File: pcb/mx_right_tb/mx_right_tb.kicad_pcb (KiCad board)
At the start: 2 copper layers, 134.9 x 113.3 mm, 60 parts, among them SW1 SW_PUSH, SW10 SW_PUSH, SW11 SW_PUSH, SW12 SW_PUSH, SW13 SW_PUSH, SW14 SW_PUSH, SW15 SW_PUSH, SW16 SW_PUSH, SW17 SW_PUSH, SW18 SW_PUSH, SW19 SW_PUSH, SW2 SW_PUSH, SW20 SW_PUSH, SW21 SW_PUSH, SW22 SW_PUSH, SW23 SW_PUSH, SW24 SW_PUSH, SW27 SW_PUSH, SW28 SW_PUSH, SW29 SW_PUSH, SW3 SW_PUSH, SW30 SW_PUSH, SW32 SW_SPDT, SW4 SW_PUSH, SW5 SW_PUSH, SW6 SW_PUSH, SW7 SW_PUSH, SW8 SW_PUSH, SW9 SW_PUSH

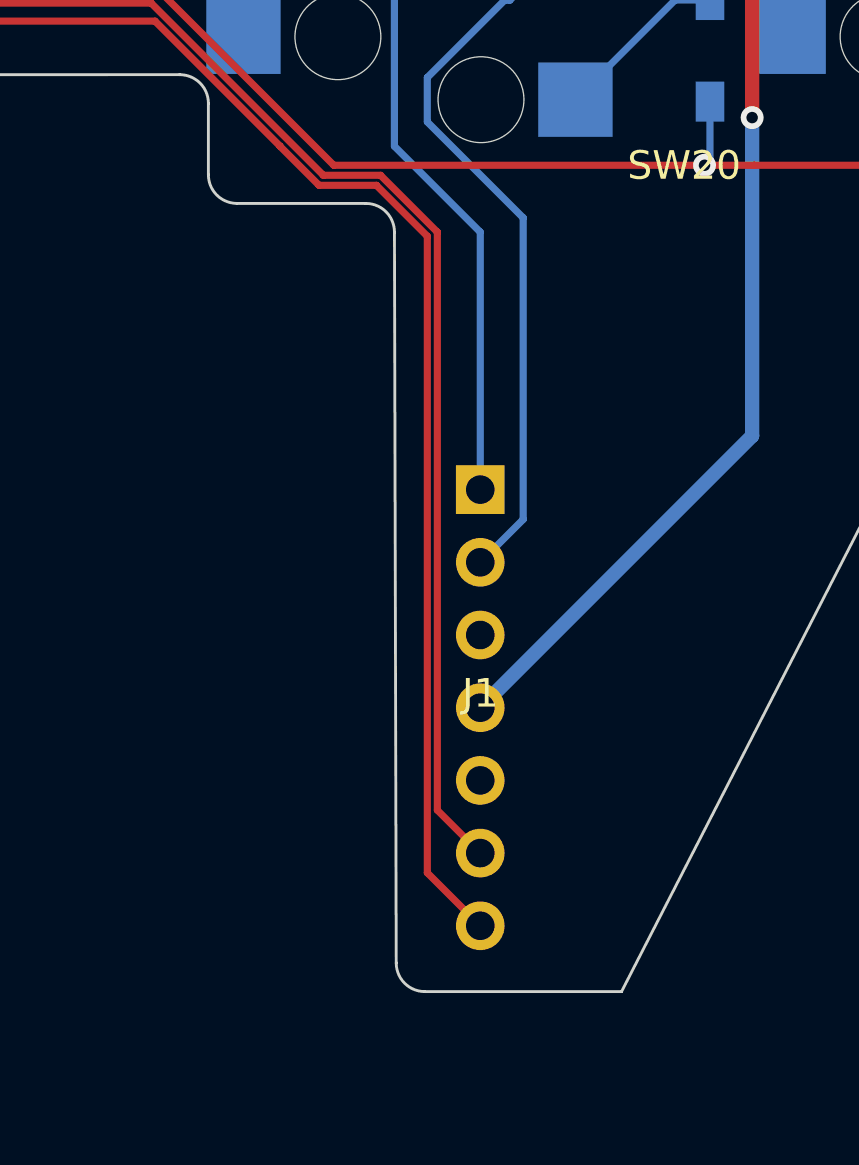
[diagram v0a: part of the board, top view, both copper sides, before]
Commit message: fix: right PCB tongue clears the trackball leg; drop thin case strips around the trackball
- right PCB: J1 tongue left edge x 158.0 -> 158.9 (trackball case leg arm overlapped 0.49 mm),
  SDIO / MOTION traces moved 0.32 right; DRC unchanged
- right case: no top case between the trackball and row 4 (2-4 mm strips, hard to print);
  parts thinner than 3 mm (top) / 2 mm (bottom) near the trackball are cut; thumb rim 4 -> 5.5 mm

Co-Authored-By: Claude Opus 5.5 <noreply@anthropic.com>
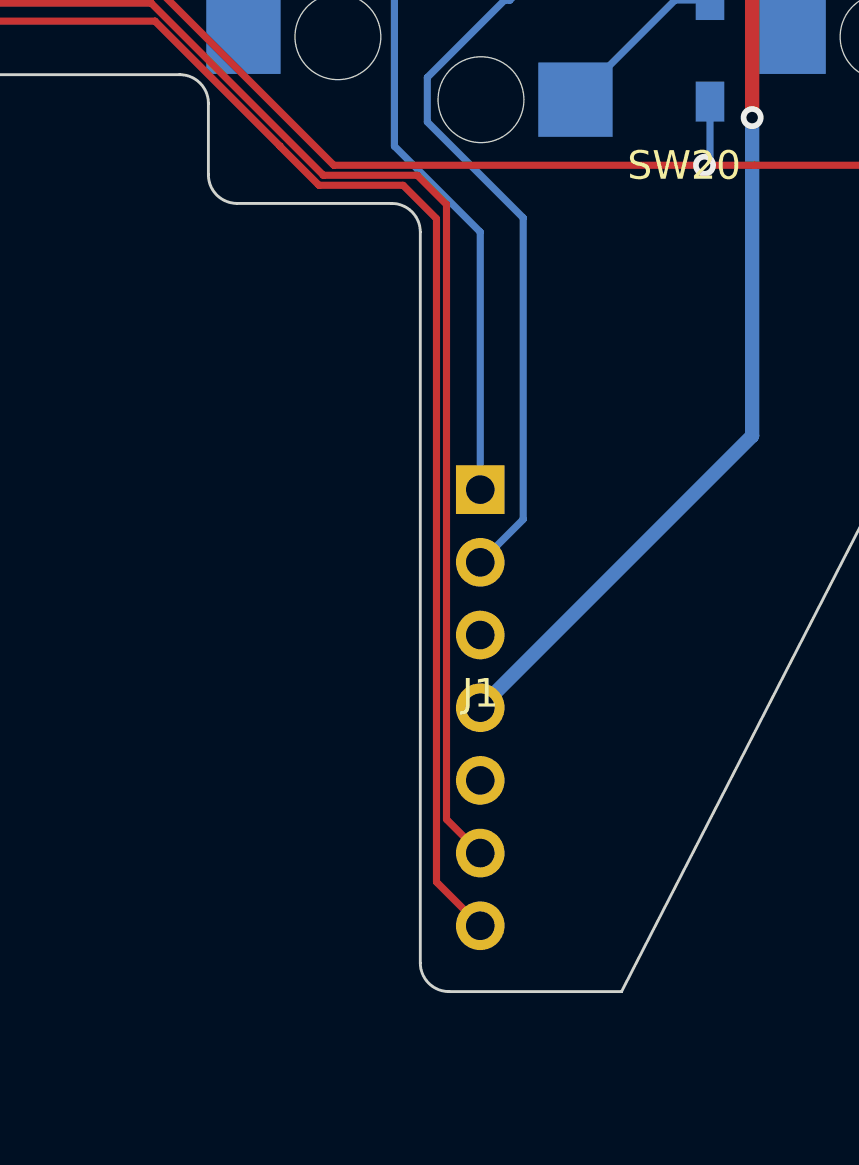
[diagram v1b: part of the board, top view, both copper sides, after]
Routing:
- net SDIO: track 164.4 -> 165.2 mm
- net MOTION: track 162.7 -> 163.2 mm
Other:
- outline, holes or cut-outs redrawn
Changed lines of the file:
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@@
 	)
 	(gr_line
-		(start 156.9965 104.775)
+		(start 157.9 104.775)
 		(end 152.495 104.775)
 		(stroke
@@
 	)
 	(gr_arc
-		(start 156.9965 104.775)
-		(mid 157.703607 105.067893)
-		(end 157.9965 105.775)
+		(start 157.9 104.775)
+		(mid 158.607107 105.067893)
+		(end 158.9 105.775)
 		(stroke
 			(width 0.1)
@@
 	)
 	(gr_line
-		(start 157.9965 105.775)
-		(end 158.058367 131.315)
+		(start 158.9 105.775)
+		(end 158.9 131.315)
 		(stroke
 			(width 0.1)
@@
 	)
 	(gr_arc
-		(start 159.058367 132.315)
-		(mid 158.35126 132.022107)
-		(end 158.058367 131.315)
+		(start 159.9 132.315)
+		(mid 159.192893 132.022107)
+		(end 158.9 131.315)
 		(stroke
 			(width 0.1)
@@
 	(gr_line
 		(start 165.931632 132.315)
-		(end 159.058367 132.315)
+		(end 159.9 132.315)
 		(stroke
 			(width 0.1)
@@
 	)
 	(segment
-		(start 159.495 105.775)
-		(end 159.495 125.975)
+		(start 159.815 104.811493)
+		(end 159.815 126.295)
 		(width 0.25)
 		(layer "F.Cu")
@@
 	)
 	(segment
-		(start 159.495 125.975)
+		(start 159.815 126.295)
 		(end 160.995 127.475)
 		(width 0.25)
@@
 	)
 	(segment
-		(start 157.511493 103.791493)
-		(end 159.495 105.775)
+		(start 158.795 103.791493)
+		(end 159.815 104.811493)
 		(width 0.25)
 		(layer "F.Cu")
@@
 	(segment
 		(start 155.511493 103.791493)
-		(end 157.511493 103.791493)
+		(end 158.795 103.791493)
 		(width 0.25)
 		(layer "F.Cu")
@@
 	)
 	(segment
-		(start 159.145 128.165)
+		(start 159.465 128.485)
 		(end 160.995 130.015)
 		(width 0.25)
@@
 	)
 	(segment
-		(start 157.366519 104.141493)
-		(end 159.145 105.919974)
+		(start 158.3 104.141493)
+		(end 159.465 105.306493)
 		(width 0.25)
 		(layer "F.Cu")
@@
 	(segment
 		(start 155.361493 104.141493)
-		(end 157.366519 104.141493)
+		(end 158.3 104.141493)
 		(width 0.25)
 		(layer "F.Cu")
@@
 	)
 	(segment
-		(start 159.145 105.919974)
-		(end 159.145 128.165)
+		(start 159.465 105.306493)
+		(end 159.465 128.485)
 		(width 0.25)
 		(layer "F.Cu")

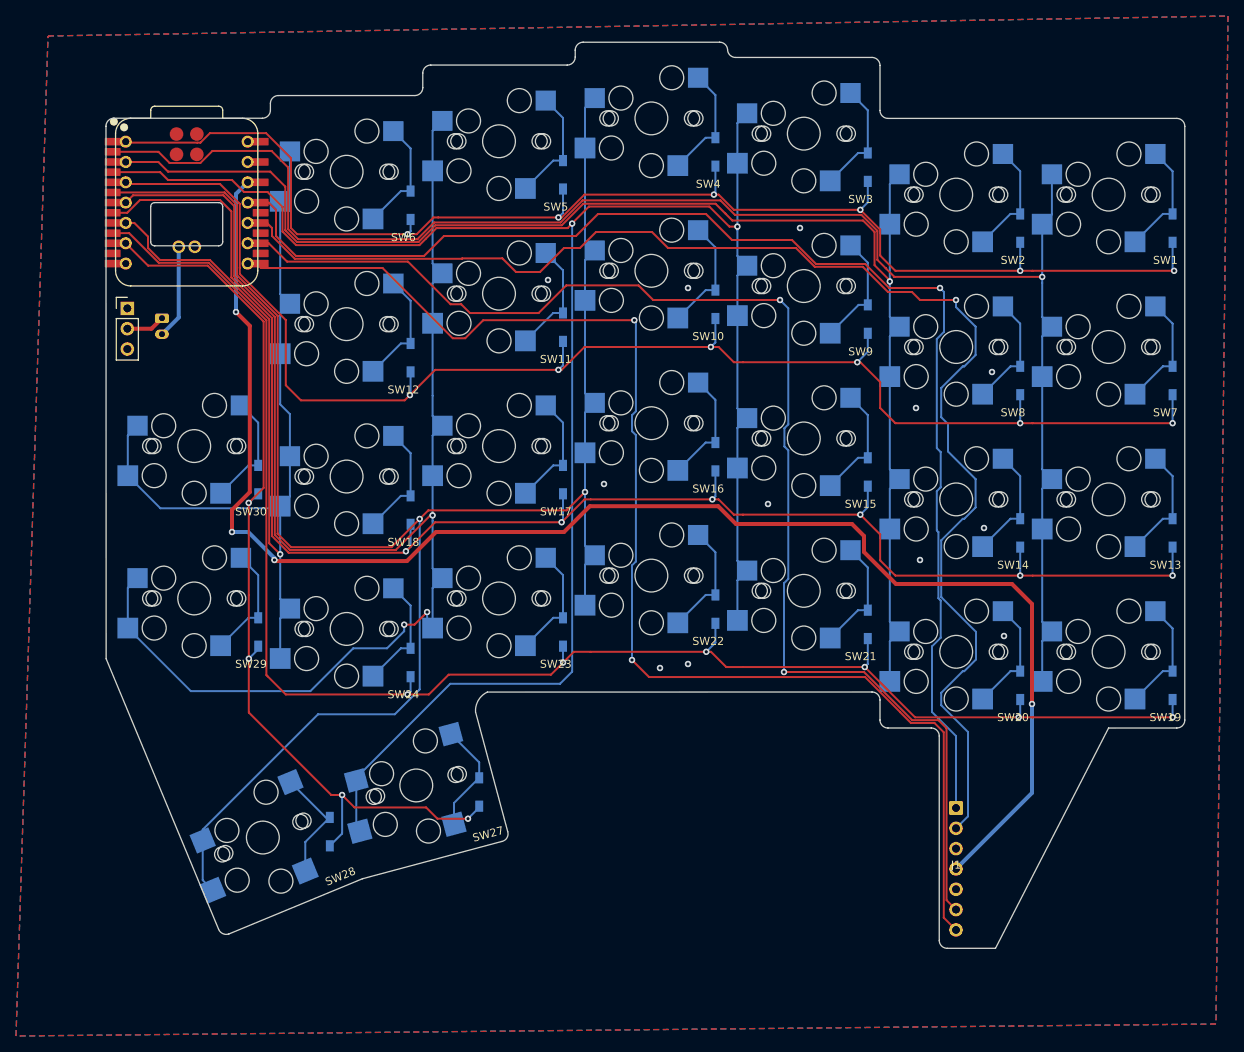
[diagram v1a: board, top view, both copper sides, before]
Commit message: fix: right PCB tongue edge 1 mm away from the trackball sensor board
tongue_trim.py: the J1 tongue's left edge x 158.9 -> 159.9; SDIO / MOTION
rerouted right of J1 (MOTION via to B.Cu), two GND stitching vias; zones refilled.

Co-Authored-By: Claude Opus 5.5 <noreply@anthropic.com>
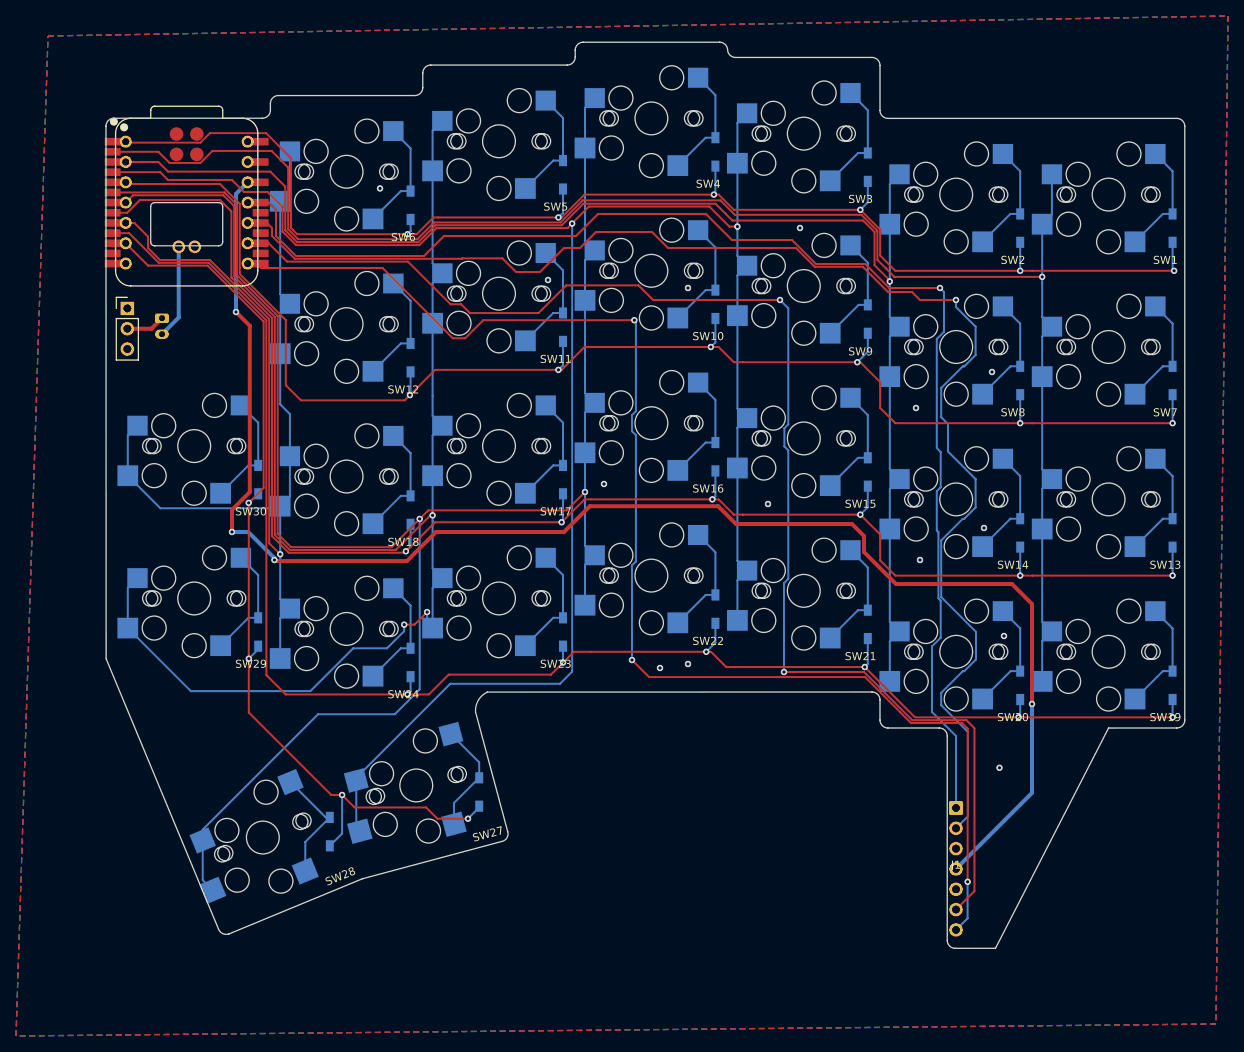
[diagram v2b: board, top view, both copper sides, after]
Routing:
- net SDIO: track 165.2 -> 169.1 mm
- net MOTION: track 163.2 -> 166.5 mm, vias 2 -> 3
- net GND: vias 12 -> 14
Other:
- outline, holes or cut-outs redrawn
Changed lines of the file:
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@@
 	)
 	(gr_line
-		(start 157.9 104.775)
+		(start 158.9 104.775)
 		(end 152.495 104.775)
 		(stroke
@@
 	)
 	(gr_arc
-		(start 157.9 104.775)
-		(mid 158.607107 105.067893)
-		(end 158.9 105.775)
+		(start 158.9 104.775)
+		(mid 159.607107 105.067893)
+		(end 159.9 105.775)
 		(stroke
 			(width 0.1)
@@
 	)
 	(gr_line
-		(start 158.9 105.775)
-		(end 158.9 131.315)
+		(start 159.9 105.775)
+		(end 159.9 131.315)
 		(stroke
 			(width 0.1)
@@
 	)
 	(gr_arc
-		(start 159.9 132.315)
-		(mid 159.192893 132.022107)
-		(end 158.9 131.315)
+		(start 160.9 132.315)
+		(mid 160.192893 132.022107)
+		(end 159.9 131.315)
 		(stroke
 			(width 0.1)
@@
 	(gr_line
 		(start 165.931632 132.315)
-		(end 159.9 132.315)
+		(end 160.9 132.315)
 		(stroke
 			(width 0.1)
@@
 	)
 	(via
+		(at 166.43 109.75)
+		(size 0.8)
+		(drill 0.4)
+		(layers "F.Cu" "B.Cu")
+		(net "GND")
+	)
+	(via
 		(at 155.995 64.775)
 		(size 0.8)
@@
 	)
 	(via
+		(at 89 37.33)
+		(size 0.8)
+		(drill 0.4)
+		(layers "F.Cu" "B.Cu")
+		(net "GND")
+	)
+	(via
 		(at 116.995 74.275)
 		(size 0.8)
@@
 	)
 	(segment
+		(start 163.3 104.791493)
+		(end 163.3 125.17)
+		(width 0.25)
+		(layer "F.Cu")
+		(net "SDIO")
+	)
+	(segment
 		(start 100.24665 52.9075)
 		(end 108.818833 52.9075)
@@
 	)
 	(segment
-		(start 159.815 104.811493)
-		(end 159.815 126.295)
+		(start 162.3 103.791493)
+		(end 163.3 104.791493)
 		(width 0.25)
 		(layer "F.Cu")
@@
 	)
 	(segment
-		(start 159.815 126.295)
-		(end 160.995 127.475)
+		(start 155.511493 103.791493)
+		(end 158.795 103.791493)
 		(width 0.25)
 		(layer "F.Cu")
@@
 	)
 	(segment
-		(start 158.795 103.791493)
-		(end 159.815 104.811493)
+		(start 112.276333 49.45)
+		(end 121.315532 49.45)
 		(width 0.25)
 		(layer "F.Cu")
@@
 	)
 	(segment
-		(start 155.511493 103.791493)
-		(end 158.795 103.791493)
+		(start 163.3 125.17)
+		(end 160.995 127.475)
 		(width 0.25)
 		(layer "F.Cu")
@@
 	)
 	(segment
-		(start 112.276333 49.45)
-		(end 121.315532 49.45)
+		(start 158.795 103.791493)
+		(end 162.3 103.791493)
 		(width 0.25)
 		(layer "F.Cu")
@@
 	)
 	(segment
-		(start 159.465 128.485)
-		(end 160.995 130.015)
+		(start 120.495 96.275)
+		(end 122.624993 98.404993)
 		(width 0.25)
 		(layer "F.Cu")
@@
 	)
 	(segment
-		(start 120.495 96.275)
-		(end 122.624993 98.404993)
+		(start 158.3 104.141493)
+		(end 161.75 104.141493)
 		(width 0.25)
 		(layer "F.Cu")
@@
 	)
 	(segment
-		(start 158.3 104.141493)
-		(end 159.465 105.306493)
+		(start 101.902254 53.801896)
+		(end 120.787904 53.801896)
 		(width 0.25)
 		(layer "F.Cu")
@@
 	)
 	(segment
-		(start 101.902254 53.801896)
-		(end 120.787904 53.801896)
+		(start 161.75 104.141493)
+		(end 162.45 104.841493)
 		(width 0.25)
 		(layer "F.Cu")
@@
 	)
 	(segment
-		(start 159.465 105.306493)
-		(end 159.465 128.485)
+		(start 153.995 102.775)
+		(end 155.361493 104.141493)
 		(width 0.25)
 		(layer "F.Cu")
@@
 	)
 	(segment
-		(start 153.995 102.775)
-		(end 155.361493 104.141493)
+		(start 162.45 104.841493)
+		(end 162.45 124)
 		(width 0.25)
 		(layer "F.Cu")
@@
 	)
 	(via
+		(at 162.45 124)
+		(size 0.8)
+		(drill 0.4)
+		(layers "F.Cu" "B.Cu")
+		(net "MOTION")
+	)
+	(via
 		(at 120.787904 53.801896)
 		(size 0.8)
@@
 	)
 	(segment
+		(start 162.45 128.56)
+		(end 160.995 130.015)
+		(width 0.25)
+		(layer "B.Cu")
+		(net "MOTION")
+	)
+	(segment
 		(start 120.985 53.998992)
 		(end 120.787904 53.801896)
 		(width 0.25)
 		(layer "B.Cu")
+		(net "MOTION")
+	)
+	(segment
+		(start 162.45 124)
+		(end 162.45 128.56)
+		(width 0.25)
+		(layer "B.Cu")
